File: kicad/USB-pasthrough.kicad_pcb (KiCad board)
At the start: 4 copper layers, 40 x 80 mm, 96 parts, among them J1 USB_Power, J10 MicroSD, J2 USB_C, J3 Power_Sel, J4 Cortex Debug, J5 SPI Display, J6 SWD, J7 Serial, J8 USB_A, J9 SD-1-A, SW1 Boot0, SW2 Reset, U1 AMS1117, U2 STM32F723VET6, Y1 8 MHz

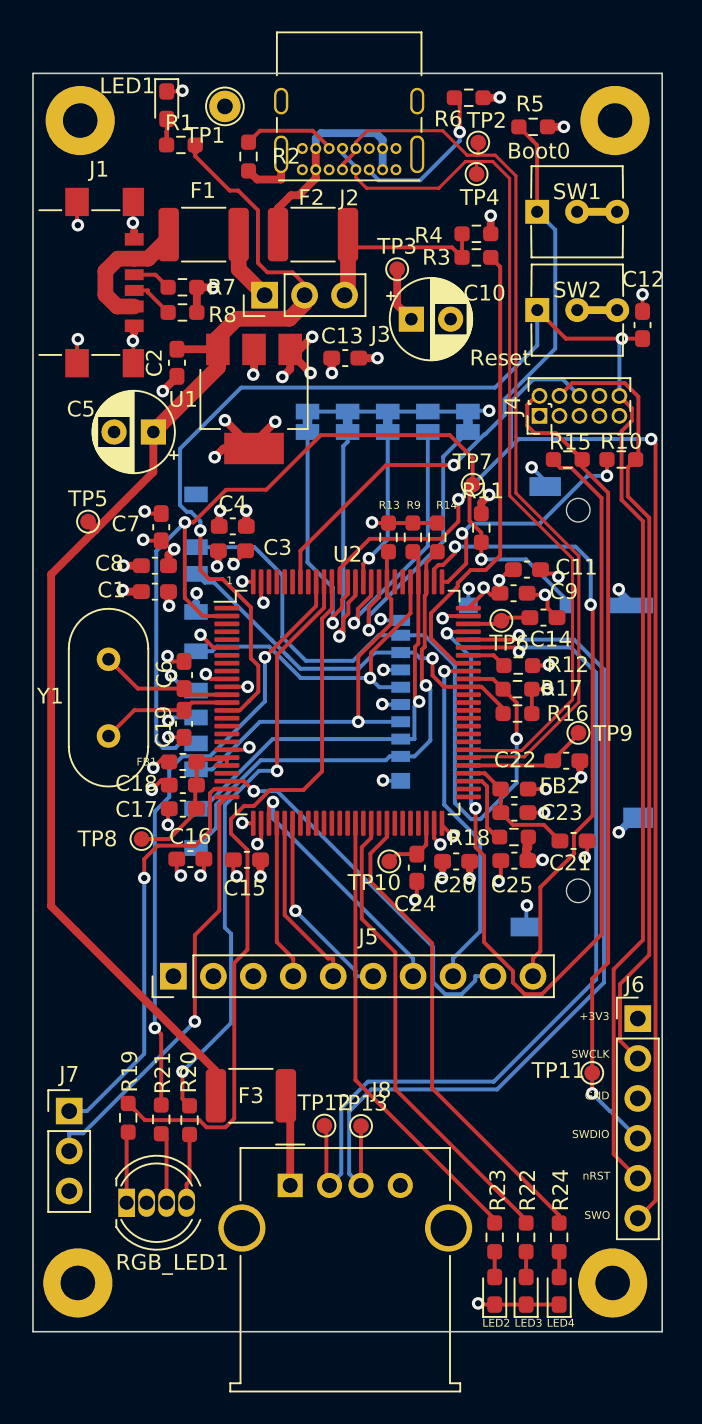
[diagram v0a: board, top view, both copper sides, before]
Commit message: Schematic and Layout for v0.2
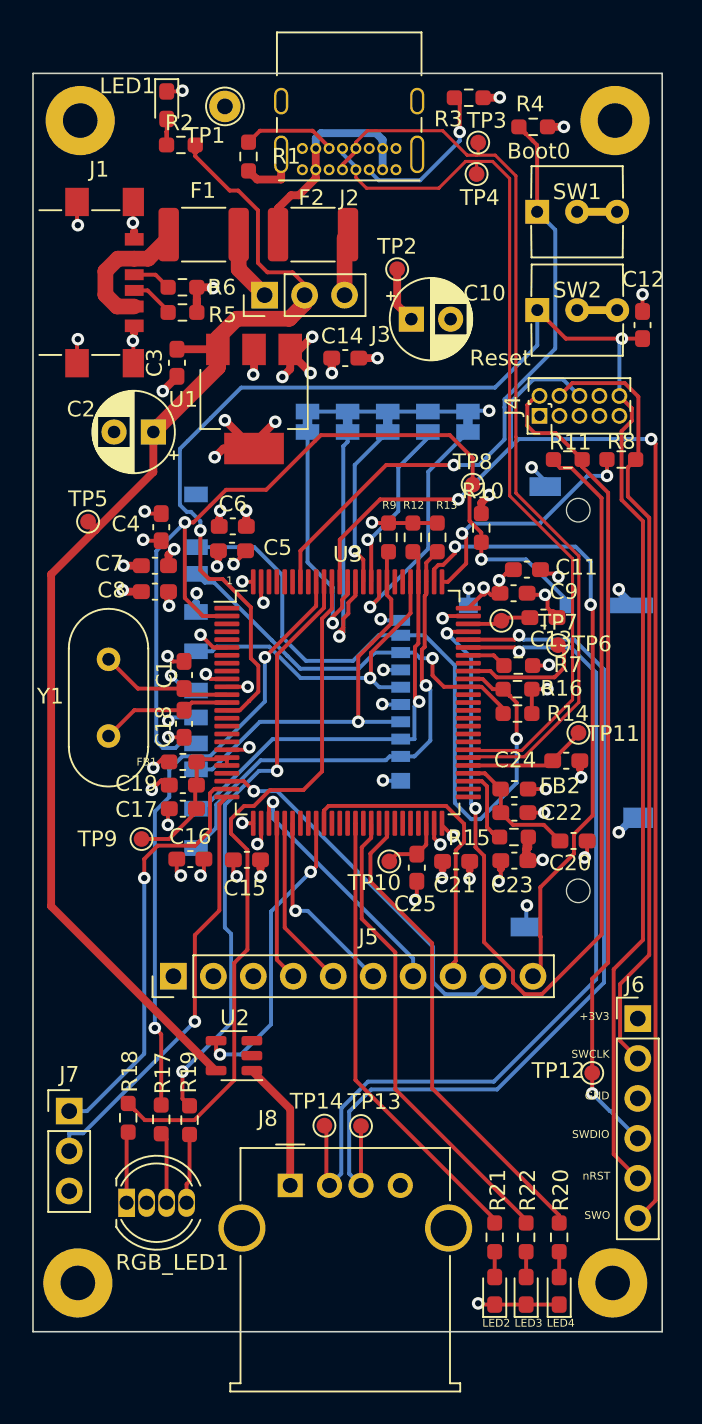
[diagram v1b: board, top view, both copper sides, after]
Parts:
- removed F3: F, Fuse:Fuse_1812_4532Metric_Pad1.30x3.40mm_HandSolder
- removed the R3 at (128.2, 61.7)
- removed the R4 at (128.2, 60.2)
- added TP7: PA8, TestPoint:TestPoint_Pad_D1.0mm, F.Cu at (133.4, 86.3)
- added U2: TPS2065C, Package_TO_SOT_SMD:SOT-23-5, F.Cu at (112.8, 112.5)
- renumbered C6 to C1, C14 to C13, C13 to C14, C19 to C18, C18 to C19, C5 to C2, C21 to C20, C20 to C21, C23 to C22, C25 to C23, C22 to C24, C24 to C25, C2 to C3, C7 to C4, C3 to C5, C4 to C6, C8 to C7, C1 to C8, R2 to R1, R11 to R10, R15 to R11, R9 to R12, R14 to R13, R16 to R14, R18 to R15, R17 to R16, R21 to R17, R19 to R18, R20 to R19, R1 to R2, R24 to R20, R23 to R21, R6 to R3, R5 to R4, R8 to R5, R7 to R6, R12 to R7, R10 to R8, R13 to R9, TP9 to TP11, TP11 to TP12, TP12 to TP14, TP3 to TP2, TP2 to TP3, TP7 to TP8, TP8 to TP9, U2 to U3
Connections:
- U3 pad 34: unconnected-(U2-Pad34) -> /USBA_ENA
- U3 pad 35: unconnected-(U2-Pad35) -> /LCD_DC
- U3 pad 67: /LCD_DC -> Net-(U3-Pad67)
- U3 pad 68: Net-(R3-Pad2) -> unconnected-(U3-Pad68)
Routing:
- net Net-(R3-Pad2): track 29.9 -> 0.00 mm
- net /USBA_ENA: track 0.00 -> 19.0 mm, vias 0 -> 2
- net /VBUS_DATA: track 13.0 -> 3.94 mm
- net Net-(U3-Pad67): track 0.00 -> 8.09 mm
- net Net-(ID2-Pad1): track 17.2 -> 11.3 mm
- net Net-(ID1-Pad1): track 18.6 -> 15.5 mm
- net Net-(J8-Pad1): track 5.81 -> 8.31 mm
- net /LCD_DC: track 22.6 -> 20.3 mm, vias 1 -> 0
- net +5V: track 81.2 -> 79.7 mm
- net /LED5_R: track 46.8 -> 45.2 mm
- net Net-(R4-Pad1): track 39.1 -> 40.7 mm
- net /SWDIO: track 53.1 -> 52.2 mm
- net Net-(LED1-Pad2): track 2.89 -> 2.10 mm
- net +3V3: track 50.5 -> 51.3 mm
- net /SD1_D1: track 46.1 -> 46.7 mm
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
